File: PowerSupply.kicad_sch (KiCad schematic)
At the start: 19 parts, among them Q1 Q_PMOS_GDS, U1 LM25085

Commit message: Second commit
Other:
- note added: "Low ESR cap."

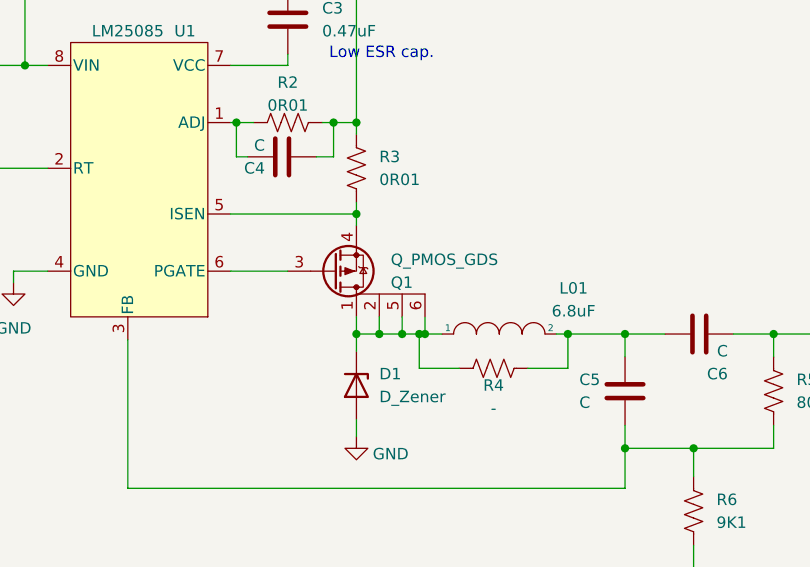
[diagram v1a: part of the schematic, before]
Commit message: PMOS update
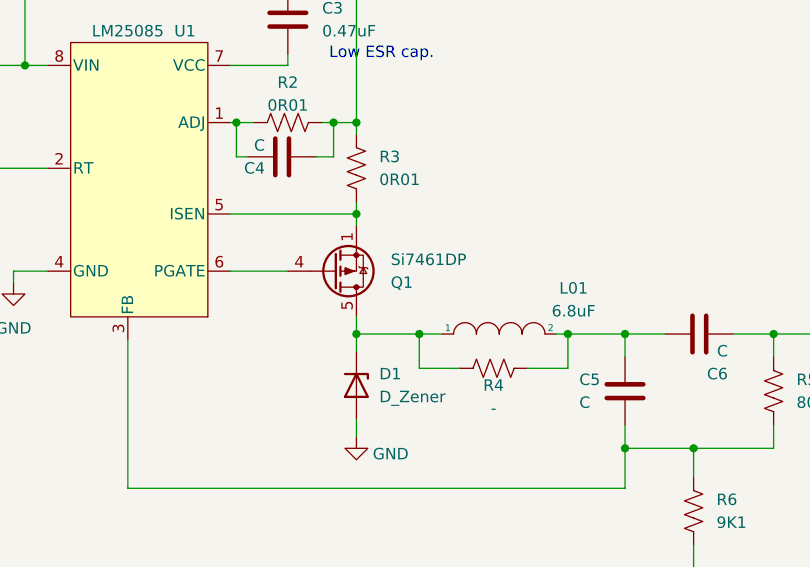
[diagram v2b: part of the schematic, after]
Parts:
- Q1: value Q_PMOS_GDS -> Si7461DP
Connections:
- net at R3.2, U1.5 (ISEN): now also Q1.1 (S), Q1.2 (S), Q1.3 (S); no longer Q1.4 (S)
- net at D1.1 (K), L01.1, Q1.5 (D)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: now also Q1.7 (D), Q1.8 (D); no longer Q1.1 (D), Q1.2 (D)
- net at U1.6 (PGATE): now also Q1.4 (G); no longer Q1.3 (G)
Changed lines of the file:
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@@
 	(paper "A4")
 	(junction
-		(at 125.73 107.315)
-		(diameter 0)
-		(color 0 0 0 0)
-	)
-	(junction
-		(at 128.27 107.315)
-		(diameter 0)
-		(color 0 0 0 0)
-	)
-	(junction
 		(at 48.895 77.47)
 		(diameter 0)
@@
 	)
 	(junction
-		(at 123.19 107.315)
-		(diameter 0)
-		(color 0 0 0 0)
-	)
-	(junction
 		(at 53.975 90.17)
 		(diameter 0)
@@
 	(wire
 		(pts
-			(xy 128.27 107.315) (xy 130.175 107.315)
-		)
-		(stroke
-			(width 0)
-			(type default)
-		)
-	)
-	(wire
-		(pts
 			(xy 95.25 107.95) (xy 95.25 124.46)
 		)
@@
 	(wire
 		(pts
-			(xy 123.19 107.315) (xy 125.73 107.315)
-		)
-		(stroke
-			(width 0)
-			(type default)
-		)
-	)
-	(wire
-		(pts
 			(xy 108.585 87.63) (xy 107.315 87.63)
 		)
@@
 	(wire
 		(pts
-			(xy 125.73 107.315) (xy 127.635 107.315)
-		)
-		(stroke
-			(width 0)
-			(type default)
-		)
-	)
-	(wire
-		(pts
 			(xy 188.595 131.445) (xy 188.595 133.985)
 		)
@@
 	(wire
 		(pts
-			(xy 128.27 105.41) (xy 128.27 107.315)
-		)
-		(stroke
-			(width 0)
-			(type default)
-		)
-	)
-	(wire
-		(pts
 			(xy 107.315 87.63) (xy 107.315 83.82)
 		)
@@
 	(wire
 		(pts
-			(xy 125.73 105.41) (xy 125.73 107.315)
-		)
-		(stroke
-			(width 0)
-			(type default)
-		)
-	)
-	(wire
-		(pts
 			(xy 68.58 77.47) (xy 83.82 77.47)
 		)
@@
 	(wire
 		(pts
-			(xy 127.635 107.315) (xy 128.27 107.315)
+			(xy 127.635 107.315) (xy 130.175 107.315)
 		)
 		(stroke
@@
 	(wire
 		(pts
-			(xy 123.19 105.41) (xy 123.19 107.315)
-		)
-		(stroke
-			(width 0)
-			(type default)
-		)
-	)
-	(wire
-		(pts
 			(xy 142.875 107.315) (xy 144.145 107.315)
 		)
@@
 	(wire
 		(pts
-			(xy 120.65 107.315) (xy 123.19 107.315)
+			(xy 120.65 107.315) (xy 127.635 107.315)
 		)
 		(stroke
@@
 			)
 		)
-		(property "Value" "Q_PMOS_GDS"
+		(property "Value" "Si7461DP"
 			(at 124.46 99.0601 0)
 			(effects
@@
 		(pin "6"
 		)
+		(pin "8"
+		)
+		(pin "7"
+		)
 		(instances

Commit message: update
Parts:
- removed C1: 33uF, Capacitor_SMD:C_1206_3216Metric_Pad1.33x1.80mm_HandSolder, symbol Device:C
- removed C5: C, Capacitor_SMD:C_0805_2012Metric_Pad1.18x1.45mm_HandSolder, symbol Device:C
- removed R4: -, Resistor_SMD:R_0805_2012Metric_Pad1.20x1.40mm_HandSolder, symbol Device:R_US
- removed R7: 270, Resistor_SMD:R_0805_2012Metric_Pad1.20x1.40mm_HandSolder, symbol Device:R_US
- C2: renamed from C3; value 0.47uF -> 1uF
- C3: renamed from C4; value C -> 1nF
- C4: renamed from C7; value 22uF -> 10uF
- C5: renamed from C8; value 22uF -> 10uF
- C6: value C -> 10uF; footprint Capacitor_SMD:C_0805_2012Metric_Pad1.18x1.45mm_HandSolder -> Capacitor_SMD:C_1206_3216Metric_Pad1.33x1.80mm_HandSolder
- L01: value 6.8uF -> 15uF; footprint Inductor_SMD:L_10.4x10.4_H4.8 -> Inductor_SMD:L_Coilcraft_XAL1010-XXX
- R1: value 100K -> 255K
- R2: value 0R01 -> 2k210
- R3: footprint Resistor_SMD:R_0805_2012Metric_Pad1.20x1.40mm_HandSolder -> Resistor_SMD:R_1206_3216Metric_Pad1.30x1.75mm_HandSolder
- R4: renamed from R5; value 80K6 -> 10k
- renumbered C2 to C1, R6 to R5
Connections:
- net GND: now also C6.2, R5.2
- net Vout (12V): now also C6.1, L01.2; no longer C6.2
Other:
- moved on the sheet: C4, C5, L01, R4, R5

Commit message: Update Schm 08/21
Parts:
- C1: value 1uF -> 10uF; footprint Capacitor_SMD:C_1206_3216Metric_Pad1.33x1.80mm_HandSolder -> Capacitor_SMD:C_1210_3225Metric_Pad1.33x2.70mm_HandSolder
- C2, C3: footprint Capacitor_SMD:C_0805_2012Metric_Pad1.18x1.45mm_HandSolder -> Capacitor_SMD:C_0402_1005Metric_Pad0.74x0.62mm_HandSolder
- C4, C5, C6: footprint Capacitor_SMD:C_1206_3216Metric_Pad1.33x1.80mm_HandSolder -> Resistor_SMD:R_2816_7142Metric_Pad3.20x4.45mm_HandSolder
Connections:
- net at Q1.3 (S), R3.2, U1.5 (ISEN): no longer Q1.1 (S), Q1.2 (S)
- net at U1.6 (PGATE): now also Q1.1 (G); no longer Q1.4 (G)
- new net: D1.1 (K), L01.1, Q1.2 (D)

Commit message: Sch update 08/21
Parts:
- removed D1: D_Zener, Diode_SMD:D_SOD-323_HandSoldering, symbol Device:D_Zener
- added D1: D_Schottky, Diode_SMD:D_SMB-SMC_Universal_Handsoldering, symbol Device:D_Schottky
- Q1: footprint Package_SO:TSOP-6_1.65x3.05mm_P0.95mm -> Package_TO_SOT_SMD:TO-263-2
- U1: footprint Package_SO:VSSOP-8_3.0x3.0mm_P0.65mm -> Package_SO:VSSOP-8_3x3mm_P0.65mm
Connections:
- net GND: now also D1.1 (K)
- net at L01.1, Q1.2 (D): now also D1.2 (A)
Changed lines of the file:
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@@
 			)
 		)
-		(property "Footprint" "Package_SO:TSOP-6_1.65x3.05mm_P0.95mm"
+		(property "Footprint" "Package_TO_SOT_SMD:TO-263-2"
 			(at 120.65 116.84 0)
 			(effects
@@
 			)
 		)
-		(property "Footprint" "Package_SO:VSSOP-8_3.0x3.0mm_P0.65mm"
+		(property "Footprint" "Package_SO:VSSOP-8_3x3mm_P0.65mm"
 			(at 96.52 83.185 0)
 			(effects
@@
 	)
 	(symbol
-		(lib_id "Device:D_Zener")
-		(at 120.65 113.03 270)
-		(unit 1)
-		(exclude_from_sim no)
-		(in_bom yes)
-		(on_board yes)
-		(dnp no)
-		(fields_autoplaced yes)
-		(property "Reference" "D1"
-			(at 123.19 111.7599 90)
-			(effects
-				(font
-					(size 1.27 1.27)
-				)
-				(justify left)
-			)
-		)
-		(property "Value" "D_Zener"
-			(at 123.19 114.2999 90)
-			(effects
-				(font
-					(size 1.27 1.27)
-				)
-				(justify left)
-			)
-		)
-		(property "Footprint" "Diode_SMD:D_SOD-323_HandSoldering"
-			(at 120.65 113.03 0)
-			(effects
-				(font
-					(size 1.27 1.27)
-				)
-				(hide yes)
-			)
-		)
-		(property "Datasheet" "~"
-			(at 120.65 113.03 0)
-			(effects
-				(font
-					(size 1.27 1.27)
-				)
-				(hide yes)
-			)
-		)
-		(property "Description" ""
-			(at 120.65 113.03 0)
-			(effects
-				(font
-					(size 1.27 1.27)
-				)
-				(hide yes)
-			)
-		)
-		(pin "1"
-		)
-		(pin "2"
-		)
-		(instances
-			(project ""
-				(path "/e63e39d7-6ac0-4ffd-8aa3-1841a4541b55"
-					(reference "D1")
-					(unit 1)
-				)
-			)
-		)
-	)
-	(symbol
 		(lib_id "Device:C")
 		(at 175.26 114.3 0)
@@
 					(unit 1)
 				)
+			)
+		)
+	)
+	(symbol
+		(lib_id "Device:D_Schottky")
+		(at 120.65 113.03 90)
+		(unit 1)
+		(exclude_from_sim no)
+		(in_bom yes)
+		(on_board yes)
+		(dnp no)
+		(property "Reference" "D1"
+			(at 123.19 112.0774 90)
+			(effects
+				(font
+					(size 1.27 1.27)
+				)
+				(justify right)
+			)
+		)
+		(property "Value" "D_Schottky"
+			(at 123.19 114.6174 90)
+			(effects
+				(font
+					(size 1.27 1.27)
+				)
+				(justify right)
+			)
+		)
+		(property "Footprint" "Diode_SMD:D_SMB-SMC_Universal_Handsoldering"
+			(at 120.65 113.03 0)
+			(effects
+				(font
+					(size 1.27 1.27)
+				)
+				(hide yes)
+			)
+		)
+		(property "Datasheet" "~"
+			(at 120.65 113.03 0)
+			(effects
+				(font
+					(size 1.27 1.27)
+				)
+				(hide yes)
+			)
+		)
+		(property "Description" "SK810L-TP"
+			(at 128.778 117.094 90)
+			(effects
+				(font
+					(size 1.27 1.27)
+				)
+			)
+		)
+		(pin "1"
+		)
+		(pin "2"
+		)
+		(instances
+			(project ""
+				(path "/e63e39d7-6ac0-4ffd-8aa3-1841a4541b55"
+					(reference "D1")
+					(unit 1)
+				)

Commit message: Update 08/24
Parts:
- removed C5, C6: 10uF, Resistor_SMD:R_2816_7142Metric_Pad3.20x4.45mm_HandSolder, symbol Device:C
- C1: value 10uF -> 1uF
- C4: footprint Resistor_SMD:R_2816_7142Metric_Pad3.20x4.45mm_HandSolder -> Capacitor_SMD:C_1206_3216Metric_Pad1.33x1.80mm_HandSolder
- D1: footprint Diode_SMD:D_SMB-SMC_Universal_Handsoldering -> Diode_SMD:D_SMB
- L01: value 15uF -> 6.2uF; footprint Inductor_SMD:L_Coilcraft_XAL1010-XXX -> Inductor_SMD:L_Bourns-SRU1028_10.0x10.0mm
- Q1: value Si7461DP -> LM25085; footprint Package_TO_SOT_SMD:TO-263-2 -> Package_SO:TSOP-6_1.65x3.05mm_P0.95mm
- R1: value 255K -> 63k4
- R2: value 2k210 -> 1k430
- R5: value 9K1 -> 1k15
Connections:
- net at R3.2, U1.5 (ISEN): now also Q1.4 (S); no longer Q1.3 (S)
- net at Q1.1 (D): now also D1.2 (A), L01.1, Q1.2 (D), Q1.5 (D), Q1.6 (D); no longer U1.6 (PGATE)
- new net: Q1.3 (G), U1.6 (PGATE)

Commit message: Update 08-28
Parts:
- Q1: value LM25085 -> SQ3419AEEV
- R2: value 1k430 -> 1k4
- U1: footprint Package_SO:VSSOP-8_3x3mm_P0.65mm -> Package_SO:HVSSOP-8-1EP_3x3mm_P0.65mm_EP1.57x1.89mm_ThermalVias
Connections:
- net GND: now also U1.9 (PGND)
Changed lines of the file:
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@@
+	)
+	(junction
+		(at 82.55 100.33)
+		(diameter 0)
+		(color 0 0 0 0)
 	)
 	(junction
@@
 	(wire
 		(pts
+			(xy 82.55 96.52) (xy 82.55 100.33)
+		)
+		(stroke
+			(width 0)
+			(type default)
+		)
+	)
+	(wire
+		(pts
 			(xy 57.785 77.47) (xy 57.785 80.01)
 		)
@@
 		(pts
 			(xy 106.68 83.82) (xy 107.315 83.82)
+		)
+		(stroke
+			(width 0)
+			(type default)
+		)
+	)
+	(wire
+		(pts
+			(xy 86.36 96.52) (xy 82.55 96.52)
 		)
 		(stroke
@@
 			)
 		)
-		(property "Description" "1/2W"
+		(property "Description" "1W"
 			(at 122.936 92.456 0)
 			(effects
@@
 			)
 		)
-		(property "Value" "LM25085"
+		(property "Value" "SQ3419AEEV"
 			(at 124.46 99.0601 0)
 			(effects
@@
 			)
 		)
-		(property "Footprint" "Package_SO:VSSOP-8_3x3mm_P0.65mm"
+		(property "Footprint" "Package_SO:HVSSOP-8-1EP_3x3mm_P0.65mm_EP1.57x1.89mm_ThermalVias"
 			(at 96.52 83.185 0)
 			(effects
@@
 		)
 		(pin "8"
+		)
+		(pin "9"
 		)
 		(instances
@@
 			)
 		)
-		(property "Value" "1k430"
+		(property "Value" "1k4"
 			(at 113.03 81.915 90)
 			(effects

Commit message: Update 08-28
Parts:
- C1: LCSC Part # (none) -> C577270; MFR Part # (none) -> CC1210KKX7R0BB105
- C2: LCSC Part # (none) -> C1518208; MFR Part # (none) -> GRM155R61H105KE05D
- C3: LCSC Part # (none) -> C76947; MFR Part # (none) -> GRM1555C1H102JA01D
- C4: LCSC Part # (none) -> C2158829; MFR Part # (none) -> TCJA106M025R0150E
- D1: footprint Diode_SMD:D_SMB -> Diode_SMD:D_SMC; LCSC Part # (none) -> C64338; MFR Part # (none) -> SK86C
- L01: LCSC Part # (none) -> C7084591; MFR Part # (none) -> SRU1038-6R2Y
- Q1: LCSC Part # (none) -> C2650243; MFR Part # (none) -> LM25085MY/NOPB
- R1: LCSC Part # (none) -> C2933483; MFR Part # (none) -> FRC0805F6342TS
- R2: LCSC Part # (none) -> C2930161; MFR Part # (none) -> FRC0805F1401TS
- R3: LCSC Part # (none) -> C2903499; MFR Part # (none) -> HoJLR1206-1W-10mR-1%
- R4: LCSC Part # (none) -> C2930231; MFR Part # (none) -> FRC0805J103TS
- R5: LCSC Part # (none) -> C3016680; MFR Part # (none) -> SCR0805F1K15
- U1: LCSC Part # (none) -> C727535; MFR Part # (none) -> SQ3419AEEV-T1_GE3
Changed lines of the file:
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@@
+			)
+		)
+		(property "LCSC Part #" "C2903499"
+			(at 120.65 88.9 0)
+			(effects
+				(font
+					(size 1.27 1.27)
+				)
+				(hide yes)
+			)
+		)
+		(property "MFR Part #" "HoJLR1206-1W-10mR-1%"
+			(at 120.65 88.9 0)
+			(effects
+				(font
+					(size 1.27 1.27)
+				)
+				(hide yes)
 			)
 		)
@@
 			)
 		)
+		(property "LCSC Part #" "C1518208 "
+			(at 113.03 72.39 0)
+			(effects
+				(font
+					(size 1.27 1.27)
+				)
+				(hide yes)
+			)
+		)
+		(property "MFR Part #" "GRM155R61H105KE05D"
+			(at 113.03 72.39 0)
+			(effects
+				(font
+					(size 1.27 1.27)
+				)
+				(hide yes)
+			)
+		)
 		(pin "1"
 		)
@@
 			)
 		)
+		(property "LCSC Part #" "C2650243"
+			(at 118.11 100.33 0)
+			(effects
+				(font
+					(size 1.27 1.27)
+				)
+				(hide yes)
+			)
+		)
+		(property "MFR Part #" "LM25085MY/NOPB"
+			(at 118.11 100.33 0)
+			(effects
+				(font
+					(size 1.27 1.27)
+				)
+				(hide yes)
+			)
+		)
 		(pin "1"
 		)
@@
 					(size 1.27 1.27)
 				)
+			)
+		)
+		(property "LCSC Part #" "C577270 "
+			(at 57.785 83.82 0)
+			(effects
+				(font
+					(size 1.27 1.27)
+				)
+				(hide yes)
+			)
+		)
+		(property "MFR Part #" "CC1210KKX7R0BB105"
+			(at 57.785 83.82 0)
+			(effects
+				(font
+					(size 1.27 1.27)
+				)
+				(hide yes)
 			)
 		)
@@
 			)
 		)
+		(property "LCSC Part #" "C2933483"
+			(at 68.58 82.55 0)
+			(effects
+				(font
+					(size 1.27 1.27)
+				)
+				(hide yes)
+			)
+		)
+		(property "MFR Part #" "FRC0805F6342TS"
+			(at 68.58 82.55 0)
+			(effects
+				(font
+					(size 1.27 1.27)
+				)
+				(hide yes)
+			)
+		)
 		(pin "1"
 		)
@@
 			)
 		)
+		(property "LCSC Part #" "C727535"
+			(at 96.52 93.98 0)
+			(effects
+				(font
+					(size 1.27 1.27)
+				)
+				(hide yes)
+			)
+		)
+		(property "MFR Part #" "SQ3419AEEV-T1_GE3"
+			(at 96.52 93.98 0)
+			(effects
+				(font
+					(size 1.27 1.27)
+				)
+				(hide yes)
+			)
+		)
 		(pin "1"
 		)
@@
 			)
 		)
+		(property "LCSC Part #" "C2158829"
+			(at 175.26 114.3 0)
+			(effects
+				(font
+					(size 1.27 1.27)
+				)
+				(hide yes)
+			)
+		)
+		(property "MFR Part #" "TCJA106M025R0150E"
+			(at 175.26 114.3 0)
+			(effects
+				(font
+					(size 1.27 1.27)
+				)
+				(hide yes)
+			)
+		)
 		(pin "1"
 		)
@@
 			)
 		)
+		(property "LCSC Part #" "C3016680"
+			(at 165.1 125.73 0)
+			(effects
+				(font
+					(size 1.27 1.27)
+				)
+				(hide yes)
+			)
+		)
+		(property "MFR Part #" "SCR0805F1K15"
+			(at 165.1 125.73 0)
+			(effects
+				(font
+					(size 1.27 1.27)
+				)
+				(hide yes)
+			)
+		)
 		(pin "1"
 		)
@@
 			)
 		)
+		(property "LCSC Part #" "C2930231"
+			(at 165.1 113.03 0)
+			(effects
+				(font
+					(size 1.27 1.27)
+				)
+				(hide yes)
+			)
+		)
+		(property "MFR Part #" "FRC0805J103TS"
+			(at 165.1 113.03 0)
+			(effects
+				(font
+					(size 1.27 1.27)
+				)
+				(hide yes)
+			)
+		)
 		(pin "1"
 		)
@@
 			)
 		)
+		(property "LCSC Part #" "C7084591"
+			(at 137.16 106.68 0)
+			(effects
+				(font
+					(size 1.27 1.27)
+				)
+				(hide yes)
+			)
+		)
+		(property "MFR Part #" "SRU1038-6R2Y"
+			(at 137.16 106.68 0)
+			(effects
+				(font
+					(size 1.27 1.27)
+				)
+				(hide yes)
+			)
+		)
 		(pin "1"
 		)
@@
 			)
 		)
+		(property "LCSC Part #" "C2930161"
+			(at 113.03 83.82 90)
+			(effects
+				(font
+					(size 1.27 1.27)
+				)
+				(hide yes)
+			)
+		)
+		(property "MFR Part #" "FRC0805F1401TS"
+			(at 113.03 83.82 90)
+			(effects
+				(font
+					(size 1.27 1.27)
+				)
+				(hide yes)
+			)
+		)
 		(pin "1"
 		)
@@
 			)
 		)
+		(property "LCSC Part #" "C76947"
+			(at 112.395 87.63 90)
+			(effects
+				(font
+					(size 1.27 1.27)
+				)
+				(hide yes)
+			)
+		)
+		(property "MFR Part #" "GRM1555C1H102JA01D"
+			(at 112.395 87.63 90)
+			(effects
+				(font
+					(size 1.27 1.27)
+				)
+				(hide yes)
+			)
+		)
 		(pin "1"
 		)
@@
 			)
 		)
-		(property "Footprint" "Diode_SMD:D_SMB"
+		(property "Footprint" "Diode_SMD:D_SMC"
 			(at 120.65 113.03 0)
 			(effects
@@
 			)
 		)
-		(property "Description" "STPS5L60"
+		(property "Description" "SK86C"
 			(at 128.778 117.094 90)
 			(effects
@@
 			)
 		)
+		(property "LCSC Part #" "C64338"
+			(at 120.65 113.03 90)
+			(effects
+				(font
+					(size 1.27 1.27)
+				)
+				(hide yes)
+			)
+		)
+		(property "MFR Part #" "SK86C"
+			(at 120.65 113.03 90)
+			(effects
+				(font
+					(size 1.27 1.27)
+				)
+				(hide yes)
+			)
+		)
